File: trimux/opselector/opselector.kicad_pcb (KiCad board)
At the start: 2 copper layers, 70 x 100 mm, 36 parts, among them J1 Conn_02x05_Odd_Even, J10 Conn_01x02, J11 Conn_01x03, J12 Conn_01x03, J13 Conn_01x02, J2 Conn_02x05_Odd_Even, J3 Conn_02x05_Odd_Even, J4 Conn_01x03, J5 Conn_01x03, J6 Conn_01x03, J7 Conn_01x03, J8 Conn_01x05, J9 Conn_01x01, P1 CONN_01X03, P2 CONN_01X03, P3 CONN_01X03, SW1 SW_SPDT, U1 trimux, U2 trimux, U3 trimux, U4 trimux, U5 trimux

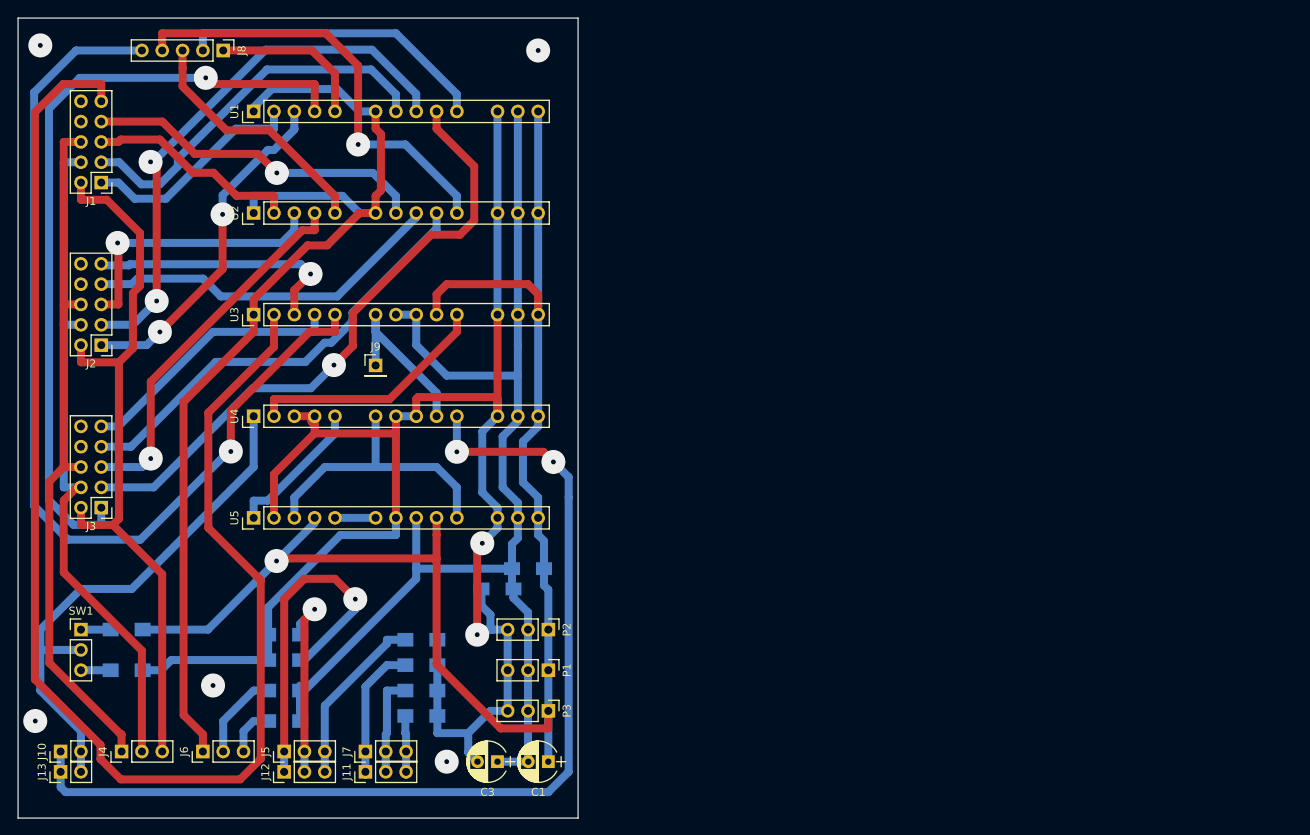
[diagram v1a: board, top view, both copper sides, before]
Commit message: opselector rerouted
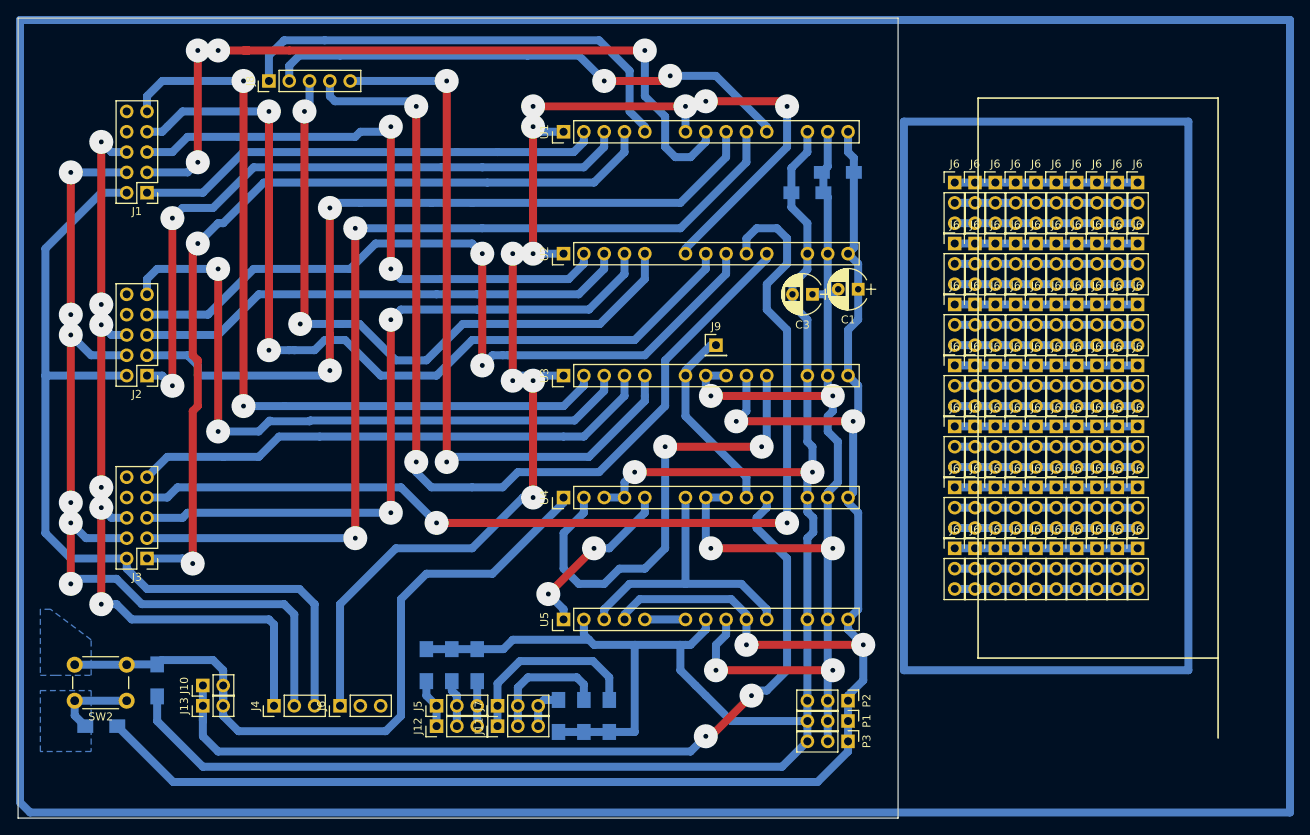
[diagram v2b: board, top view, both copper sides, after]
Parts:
- removed R1, R2: 100k, Resistors_SMD:R_1206_HandSoldering
- removed SW1: SW_SPDT, Pin_Headers:Pin_Header_Straight_1x03_Pitch2.54mm
- added J6: Conn_01x03, Pin_Headers:Pin_Header_Straight_1x03_Pitch2.54mm, F.Cu at (154.9, 35.6)
- added J6: Conn_01x03, Pin_Headers:Pin_Header_Straight_1x03_Pitch2.54mm, F.Cu at (152.4, 58.4)
- added J6: Conn_01x03, Pin_Headers:Pin_Header_Straight_1x03_Pitch2.54mm, F.Cu at (152.4, 50.8)
- added J6: Conn_01x03, Pin_Headers:Pin_Header_Straight_1x03_Pitch2.54mm, F.Cu at (152.4, 73.7)
- added J6: Conn_01x03, Pin_Headers:Pin_Header_Straight_1x03_Pitch2.54mm, F.Cu at (152.4, 81.3)
- added J6: Conn_01x03, Pin_Headers:Pin_Header_Straight_1x03_Pitch2.54mm, F.Cu at (152.4, 66.0)
- added J6: Conn_01x03, Pin_Headers:Pin_Header_Straight_1x03_Pitch2.54mm, F.Cu at (142.2, 35.6)
- added J6: Conn_01x03, Pin_Headers:Pin_Header_Straight_1x03_Pitch2.54mm, F.Cu at (142.2, 43.2)
- added J6: Conn_01x03, Pin_Headers:Pin_Header_Straight_1x03_Pitch2.54mm, F.Cu at (142.2, 58.4)
- added J6: Conn_01x03, Pin_Headers:Pin_Header_Straight_1x03_Pitch2.54mm, F.Cu at (142.2, 50.8)
- added J6: Conn_01x03, Pin_Headers:Pin_Header_Straight_1x03_Pitch2.54mm, F.Cu at (142.2, 73.7)
- added J6: Conn_01x03, Pin_Headers:Pin_Header_Straight_1x03_Pitch2.54mm, F.Cu at (154.9, 43.2)
- added J6: Conn_01x03, Pin_Headers:Pin_Header_Straight_1x03_Pitch2.54mm, F.Cu at (142.2, 81.3)
- added J6: Conn_01x03, Pin_Headers:Pin_Header_Straight_1x03_Pitch2.54mm, F.Cu at (142.2, 66.0)
- added J6: Conn_01x03, Pin_Headers:Pin_Header_Straight_1x03_Pitch2.54mm, F.Cu at (144.8, 66.0)
- added J6: Conn_01x03, Pin_Headers:Pin_Header_Straight_1x03_Pitch2.54mm, F.Cu at (144.8, 81.3)
- added J6: Conn_01x03, Pin_Headers:Pin_Header_Straight_1x03_Pitch2.54mm, F.Cu at (144.8, 73.7)
- added J6: Conn_01x03, Pin_Headers:Pin_Header_Straight_1x03_Pitch2.54mm, F.Cu at (144.8, 50.8)
- added J6: Conn_01x03, Pin_Headers:Pin_Header_Straight_1x03_Pitch2.54mm, F.Cu at (144.8, 58.4)
- added J6: Conn_01x03, Pin_Headers:Pin_Header_Straight_1x03_Pitch2.54mm, F.Cu at (144.8, 43.2)
- added J6: Conn_01x03, Pin_Headers:Pin_Header_Straight_1x03_Pitch2.54mm, F.Cu at (144.8, 35.6)
- added J6: Conn_01x03, Pin_Headers:Pin_Header_Straight_1x03_Pitch2.54mm, F.Cu at (149.9, 35.6)
- added J6: Conn_01x03, Pin_Headers:Pin_Header_Straight_1x03_Pitch2.54mm, F.Cu at (154.9, 58.4)
- added J6: Conn_01x03, Pin_Headers:Pin_Header_Straight_1x03_Pitch2.54mm, F.Cu at (149.9, 43.2)
- added J6: Conn_01x03, Pin_Headers:Pin_Header_Straight_1x03_Pitch2.54mm, F.Cu at (149.9, 58.4)
- added J6: Conn_01x03, Pin_Headers:Pin_Header_Straight_1x03_Pitch2.54mm, F.Cu at (149.9, 50.8)
- added J6: Conn_01x03, Pin_Headers:Pin_Header_Straight_1x03_Pitch2.54mm, F.Cu at (149.9, 73.7)
- added J6: Conn_01x03, Pin_Headers:Pin_Header_Straight_1x03_Pitch2.54mm, F.Cu at (149.9, 81.3)
- added J6: Conn_01x03, Pin_Headers:Pin_Header_Straight_1x03_Pitch2.54mm, F.Cu at (149.9, 66.0)
- added J6: Conn_01x03, Pin_Headers:Pin_Header_Straight_1x03_Pitch2.54mm, F.Cu at (147.3, 66.0)
- added J6: Conn_01x03, Pin_Headers:Pin_Header_Straight_1x03_Pitch2.54mm, F.Cu at (147.3, 81.3)
- added J6: Conn_01x03, Pin_Headers:Pin_Header_Straight_1x03_Pitch2.54mm, F.Cu at (147.3, 73.7)
- added J6: Conn_01x03, Pin_Headers:Pin_Header_Straight_1x03_Pitch2.54mm, F.Cu at (147.3, 50.8)
- added J6: Conn_01x03, Pin_Headers:Pin_Header_Straight_1x03_Pitch2.54mm, F.Cu at (154.9, 50.8)
- added J6: Conn_01x03, Pin_Headers:Pin_Header_Straight_1x03_Pitch2.54mm, F.Cu at (147.3, 58.4)
- added J6: Conn_01x03, Pin_Headers:Pin_Header_Straight_1x03_Pitch2.54mm, F.Cu at (147.3, 43.2)
- added J6: Conn_01x03, Pin_Headers:Pin_Header_Straight_1x03_Pitch2.54mm, F.Cu at (147.3, 35.6)
- added J6: Conn_01x03, Pin_Headers:Pin_Header_Straight_1x03_Pitch2.54mm, F.Cu at (137.2, 35.6)
- added J6: Conn_01x03, Pin_Headers:Pin_Header_Straight_1x03_Pitch2.54mm, F.Cu at (137.2, 43.2)
- added J6: Conn_01x03, Pin_Headers:Pin_Header_Straight_1x03_Pitch2.54mm, F.Cu at (137.2, 58.4)
- added J6: Conn_01x03, Pin_Headers:Pin_Header_Straight_1x03_Pitch2.54mm, F.Cu at (137.2, 50.8)
- added J6: Conn_01x03, Pin_Headers:Pin_Header_Straight_1x03_Pitch2.54mm, F.Cu at (137.2, 73.7)
- added J6: Conn_01x03, Pin_Headers:Pin_Header_Straight_1x03_Pitch2.54mm, F.Cu at (137.2, 81.3)
- added J6: Conn_01x03, Pin_Headers:Pin_Header_Straight_1x03_Pitch2.54mm, F.Cu at (137.2, 66.0)
- added J6: Conn_01x03, Pin_Headers:Pin_Header_Straight_1x03_Pitch2.54mm, F.Cu at (154.9, 73.7)
- added J6: Conn_01x03, Pin_Headers:Pin_Header_Straight_1x03_Pitch2.54mm, F.Cu at (139.7, 66.0)
- added J6: Conn_01x03, Pin_Headers:Pin_Header_Straight_1x03_Pitch2.54mm, F.Cu at (139.7, 81.3)
- added J6: Conn_01x03, Pin_Headers:Pin_Header_Straight_1x03_Pitch2.54mm, F.Cu at (139.7, 73.7)
- added J6: Conn_01x03, Pin_Headers:Pin_Header_Straight_1x03_Pitch2.54mm, F.Cu at (139.7, 50.8)
- added J6: Conn_01x03, Pin_Headers:Pin_Header_Straight_1x03_Pitch2.54mm, F.Cu at (139.7, 58.4)
- added J6: Conn_01x03, Pin_Headers:Pin_Header_Straight_1x03_Pitch2.54mm, F.Cu at (139.7, 43.2)
- added J6: Conn_01x03, Pin_Headers:Pin_Header_Straight_1x03_Pitch2.54mm, F.Cu at (139.7, 35.6)
- added J6: Conn_01x03, Pin_Headers:Pin_Header_Straight_1x03_Pitch2.54mm, F.Cu at (134.6, 35.6)
- added J6: Conn_01x03, Pin_Headers:Pin_Header_Straight_1x03_Pitch2.54mm, F.Cu at (134.6, 43.2)
- added J6: Conn_01x03, Pin_Headers:Pin_Header_Straight_1x03_Pitch2.54mm, F.Cu at (134.6, 58.4)
- added J6: Conn_01x03, Pin_Headers:Pin_Header_Straight_1x03_Pitch2.54mm, F.Cu at (154.9, 81.3)
- added J6: Conn_01x03, Pin_Headers:Pin_Header_Straight_1x03_Pitch2.54mm, F.Cu at (134.6, 50.8)
- added J6: Conn_01x03, Pin_Headers:Pin_Header_Straight_1x03_Pitch2.54mm, F.Cu at (134.6, 73.7)
- added J6: Conn_01x03, Pin_Headers:Pin_Header_Straight_1x03_Pitch2.54mm, F.Cu at (134.6, 81.3)
- added J6: Conn_01x03, Pin_Headers:Pin_Header_Straight_1x03_Pitch2.54mm, F.Cu at (134.6, 66.0)
- added J6: Conn_01x03, Pin_Headers:Pin_Header_Straight_1x03_Pitch2.54mm, F.Cu at (132.1, 66.0)
- added J6: Conn_01x03, Pin_Headers:Pin_Header_Straight_1x03_Pitch2.54mm, F.Cu at (132.1, 81.3)
- added J6: Conn_01x03, Pin_Headers:Pin_Header_Straight_1x03_Pitch2.54mm, F.Cu at (132.1, 73.7)
- added J6: Conn_01x03, Pin_Headers:Pin_Header_Straight_1x03_Pitch2.54mm, F.Cu at (132.1, 50.8)
- added J6: Conn_01x03, Pin_Headers:Pin_Header_Straight_1x03_Pitch2.54mm, F.Cu at (132.1, 58.4)
- added J6: Conn_01x03, Pin_Headers:Pin_Header_Straight_1x03_Pitch2.54mm, F.Cu at (132.1, 43.2)
- added J6: Conn_01x03, Pin_Headers:Pin_Header_Straight_1x03_Pitch2.54mm, F.Cu at (154.9, 66.0)
- added J6: Conn_01x03, Pin_Headers:Pin_Header_Straight_1x03_Pitch2.54mm, F.Cu at (132.1, 35.6)
- added J6: Conn_01x03, Pin_Headers:Pin_Header_Straight_1x03_Pitch2.54mm, F.Cu at (152.4, 35.6)
- added J6: Conn_01x03, Pin_Headers:Pin_Header_Straight_1x03_Pitch2.54mm, F.Cu at (152.4, 43.2)
- added SW2: SW_Push_Dual, Buttons_Switches_THT:SW_PUSH_6mm_h13mm, F.Cu at (28.6, 100.3)
- R9: value 100k -> 1k
- moved C1 70.6 mm to (120.0, 48.9)
- moved C3 70.4 mm to (114.3, 49.5)
- moved C4 62.9 mm to (113.7, 36.8)
- moved C2 62.9 mm to (117.5, 34.3)
- moved J9 42.6 mm to (102.2, 55.9)
- moved U5 40.8 mm to (83.2, 90.2)
- moved U4 40.0 mm to (83.2, 74.9)
- moved U3 39.5 mm to (83.2, 59.7)
- moved U2 39.1 mm to (83.2, 44.5)
- moved U1 38.8 mm to (83.2, 29.2)
- moved P2 38.5 mm to (118.7, 100.3)
- moved P1 38.0 mm to (118.7, 102.9)
- moved P3 37.7 mm to (118.7, 105.4)
- moved R3 24.3 mm to (88.9, 102.2), turned to 270 degrees
- moved R7 21.3 mm to (69.2, 95.9), turned to 90 degrees
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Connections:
- net Net-(U3-Pad11) renamed /BLOCK_NEGATIVE_CLK
- R10 pad 1: Net-(R10-Pad1) -> /RESET_COUNTER
- U4 pad 8: -5V -> GNDREF
- U4 pad 9: -5V -> GNDREF
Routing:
- net (no net): track 0.00 -> 723.2 mm, vias 5 -> 0
- net /SEGMENT_LO: track 130.5 -> 328.1 mm, vias 0 -> 10
- net /SEGMENT_HI: track 6.15 -> 160.0 mm
- net /SEGMENT_MI: track 11.0 -> 160.0 mm
- net Net-(J1-Pad9): track 179.9 -> 100.3 mm, vias 0 -> 2
- net Net-(J3-Pad7): track 55.9 -> 128.1 mm, vias 0 -> 2
- net Net-(J1-Pad7): track 42.8 -> 110.5 mm, vias 1 -> 2
- net /OPCODE_3: track 55.3 -> 119.4 mm, vias 1 -> 2
- net -5V: track 216.7 -> 280.3 mm
- net Net-(J2-Pad7): track 45.2 -> 97.8 mm, vias 0 -> 2
- net /OPCODE_2: track 31.4 -> 83.5 mm, vias 0 -> 2
- net Net-(J2-Pad9): track 32.7 -> 84.1 mm, vias 1 -> 2
- net Net-(J1-Pad3): track 47.9 -> 98.1 mm, vias 0 -> 4
- net Net-(J1-Pad5): track 26.8 -> 76.3 mm, vias 0 -> 2
- net +5V: track 187.8 -> 235.7 mm, vias 1 -> 4
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- added copper zone on B.Cu, net /RESET_COUNTER
- added copper zone on B.Cu, net Net-(R9-Pad2)
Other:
- board size 70 x 100 mm -> 110 x 100 mm
